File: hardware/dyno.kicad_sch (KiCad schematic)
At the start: 10 parts, among them J1 Battery, J2 Load cell, SW1 B3W-1000, U1 XIAO-ESP32-C3-SMD, U2 HX711

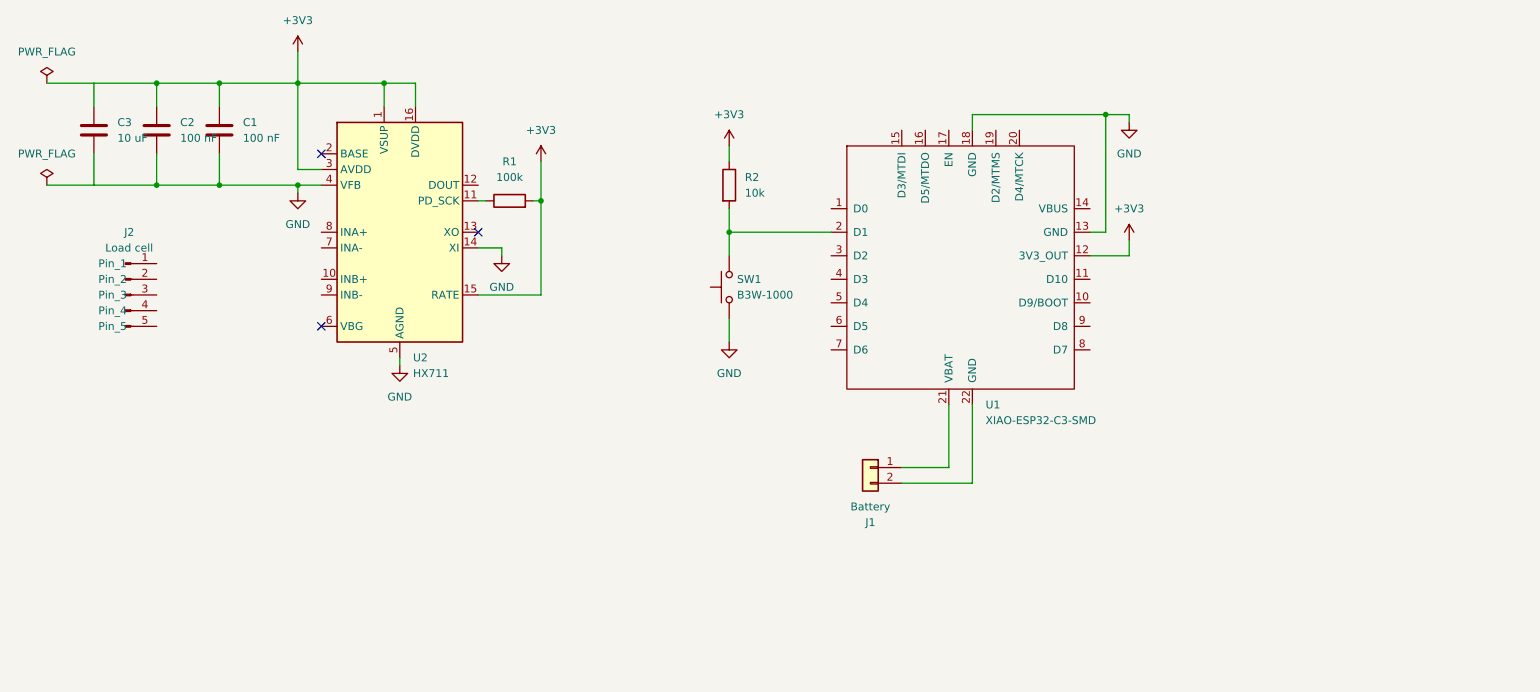
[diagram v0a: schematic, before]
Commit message: wire mcu and amp
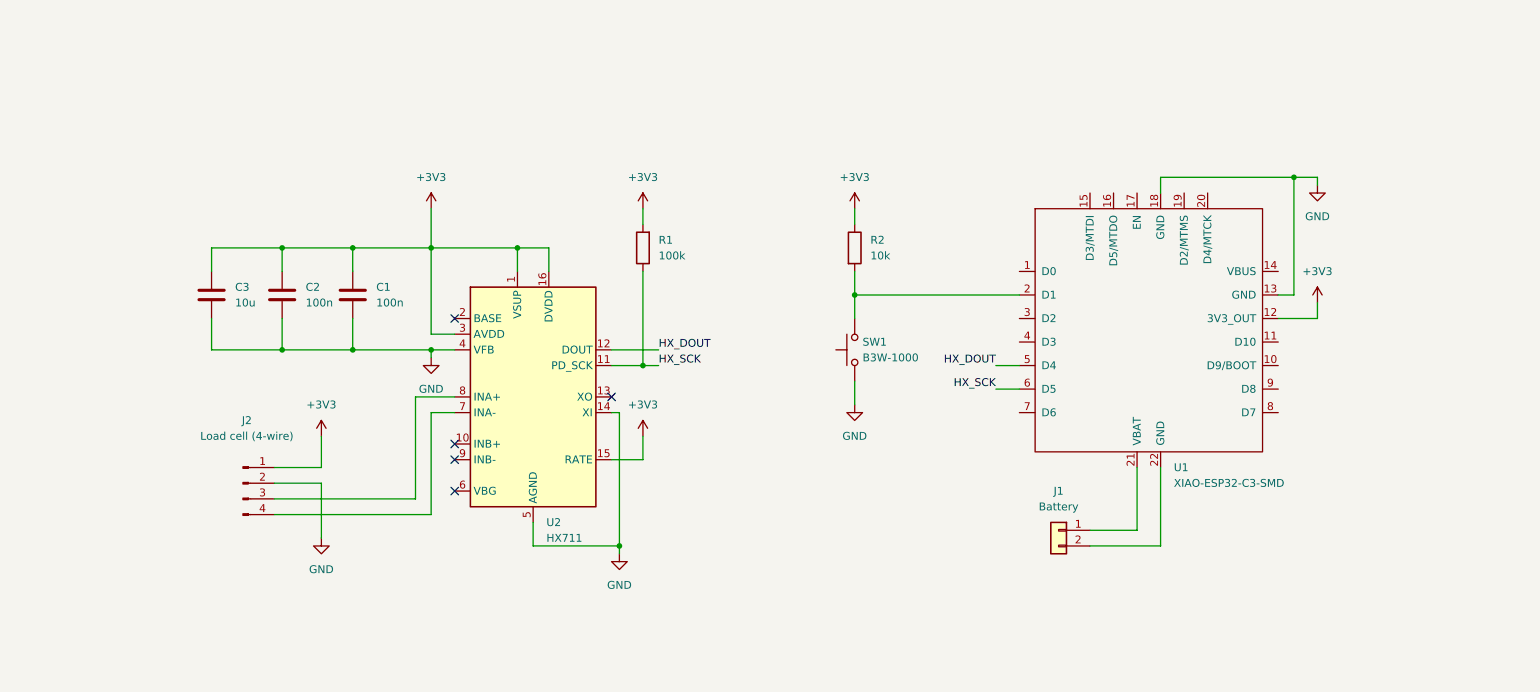
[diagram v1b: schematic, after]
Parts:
- C1, C2: value 100 nF -> 100n
- C3: value 10 uF -> 10u
- J2: value Load cell -> Load cell (4-wire); footprint (none) -> Connector_JST:JST_SH_SM04B-SRSS-TB_1x04-1MP_P1.00mm_Horizontal; symbol Connector:Conn_01x05_Pin -> Connector:Conn_01x04_Pin
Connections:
- net +3V3: now also J2.1 (Pin_1)
- net GND: now also J2.2 (Pin_2)
- net HX_SCK: now reaches R1.1, U2.11 (PD_SCK)
- net HX_SCK: now also U1.6 (D5)
- net at U2.12 (DOUT): no longer names the net of U2.12 (DOUT)
- net at U2.12 (DOUT): now also U1.5 (D4)
- net at U2.7 (INA-): now also J2.4 (Pin_4)
- net at U2.8 (INA+): now also J2.3 (Pin_3)
- no-connect marks 3 -> 5
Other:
- moved on the sheet: C1, C2, C3, J1, R1, R2, SW1, U1, U2

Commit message: fix ERC errors
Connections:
- net HX_DOUT: now reaches U1.5 (D4), U2.12 (DOUT)
- no-connect marks 5 -> 19

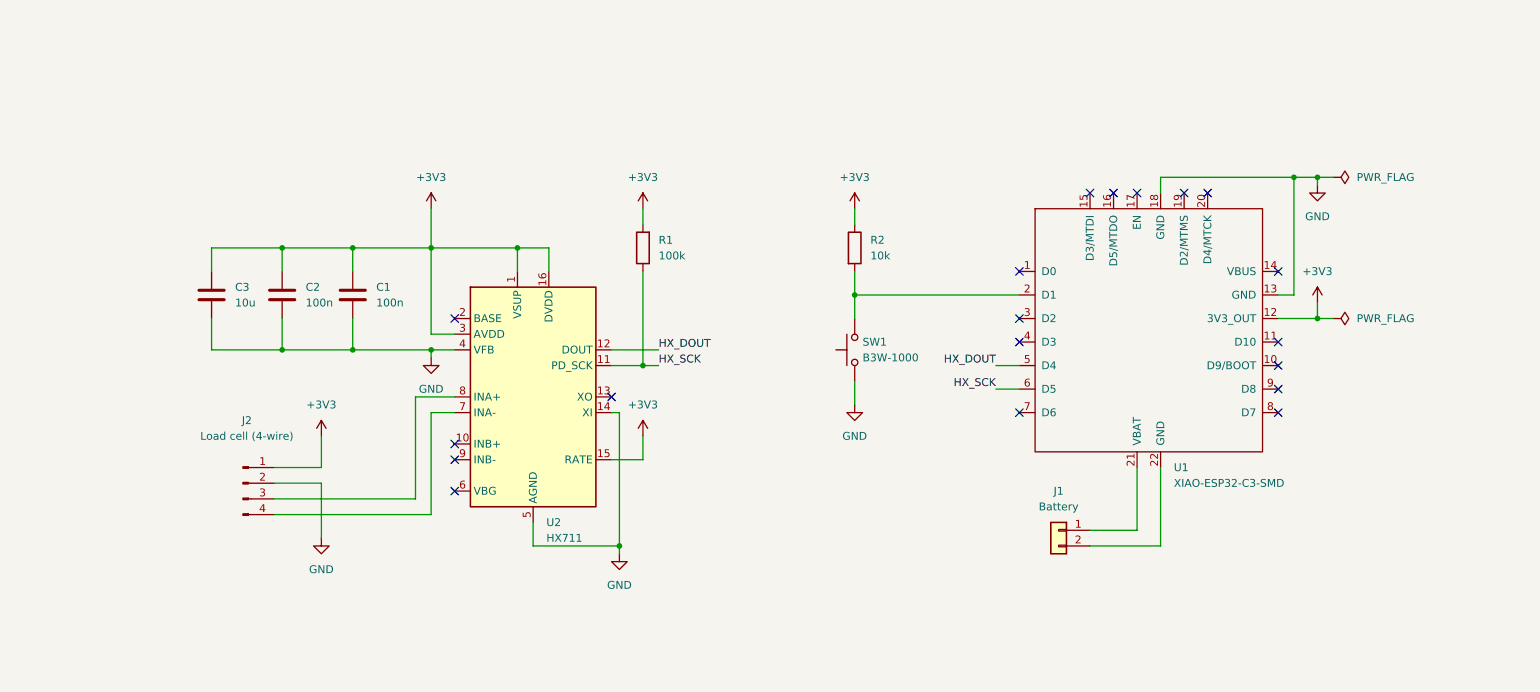
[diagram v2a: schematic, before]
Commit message: clean up schematic
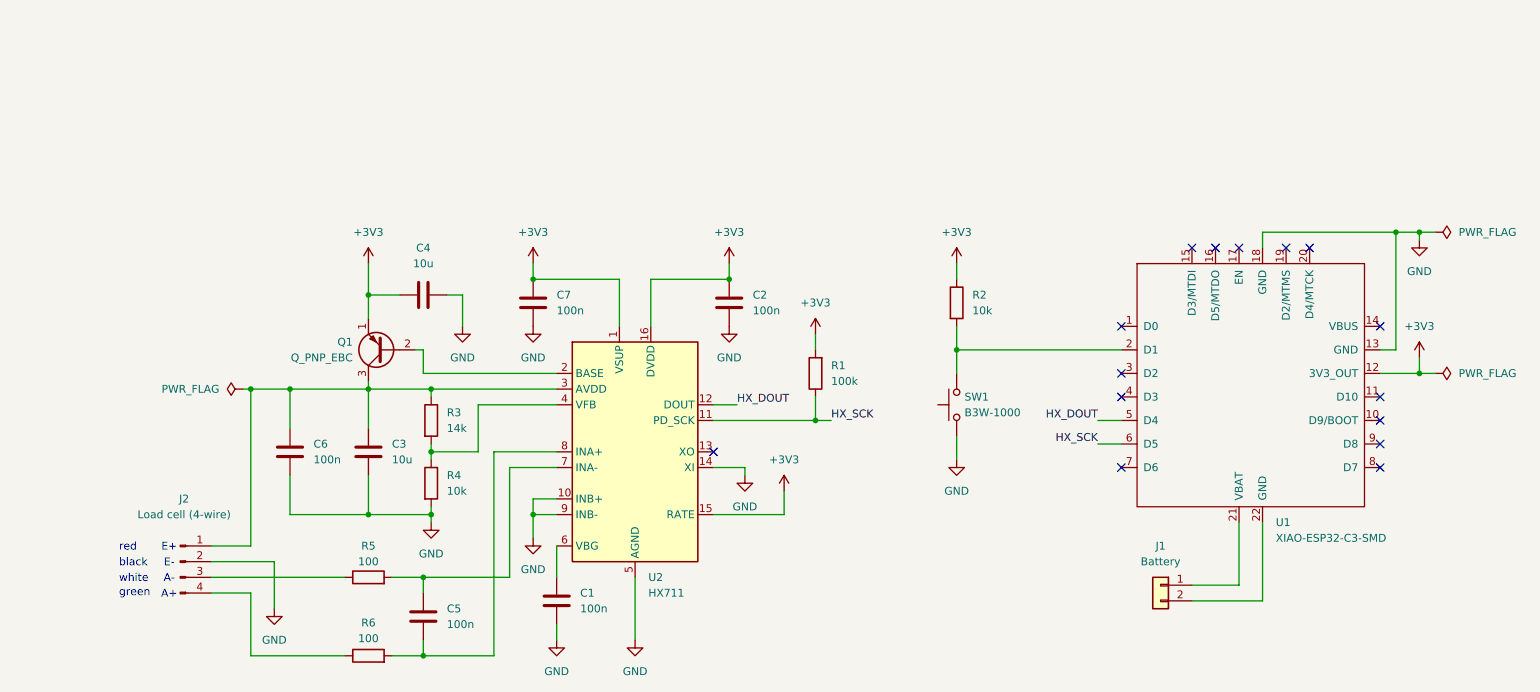
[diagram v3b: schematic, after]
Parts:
- added C4: 10u, symbol Device:C
- added C5, C6, C7: 100n, symbol Device:C
- added Q1: Q_PNP_EBC, symbol Transistor_BJT:Q_PNP_EBC
- added R3: 14k, symbol Device:R
- added R4: 10k, symbol Device:R
- added R5, R6: 100, symbol Device:R
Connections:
- net +3V3: now also C2.2, C4.1, C7.2, Q1.1 (E); no longer C1.1, C2.1, C3.1, J2.1 (Pin_1), U2.3 (AVDD)
- net GND: now also C2.1, U2.10 (INB+), U2.9 (INB-), C4.2, C6.2, C7.1, R4.2; no longer C2.2, U2.4 (VFB)
- net at U2.2 (BASE): now also Q1.2 (B)
- net at U2.6 (VBG): now also C1.1
- net at U2.7 (INA-): now also C5.1, R5.2; no longer J2.4 (Pin_4)
- net at U2.8 (INA+): now also C5.2, R6.2; no longer J2.3 (Pin_3)
- new net: C3.1, C6.1, J2.1 (Pin_1), Q1.3 (C), R3.1, U2.3 (AVDD)
- new net: R3.2, R4.1, U2.4 (VFB)
- new net: J2.3 (Pin_3), R5.1
- new net: J2.4 (Pin_4), R6.1
- no-connect marks 19 -> 15
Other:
- note added: "A+"
- note added: "A-"
- note added: "E+"
- note added: "E-"
- note added: "black"
- note added: "green"
- note added: "red"
- note added: "white"
- moved on the sheet: C1, C2, C3, J1, J2, R1, R2, SW1, U1, U2

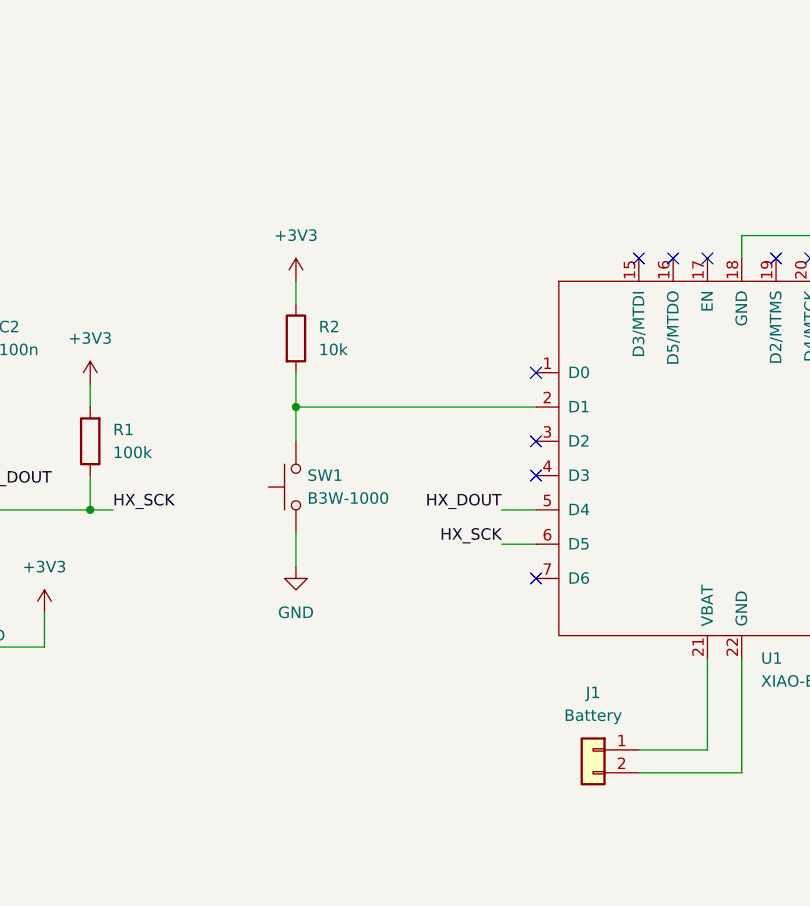
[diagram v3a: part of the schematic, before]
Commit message: add status LED
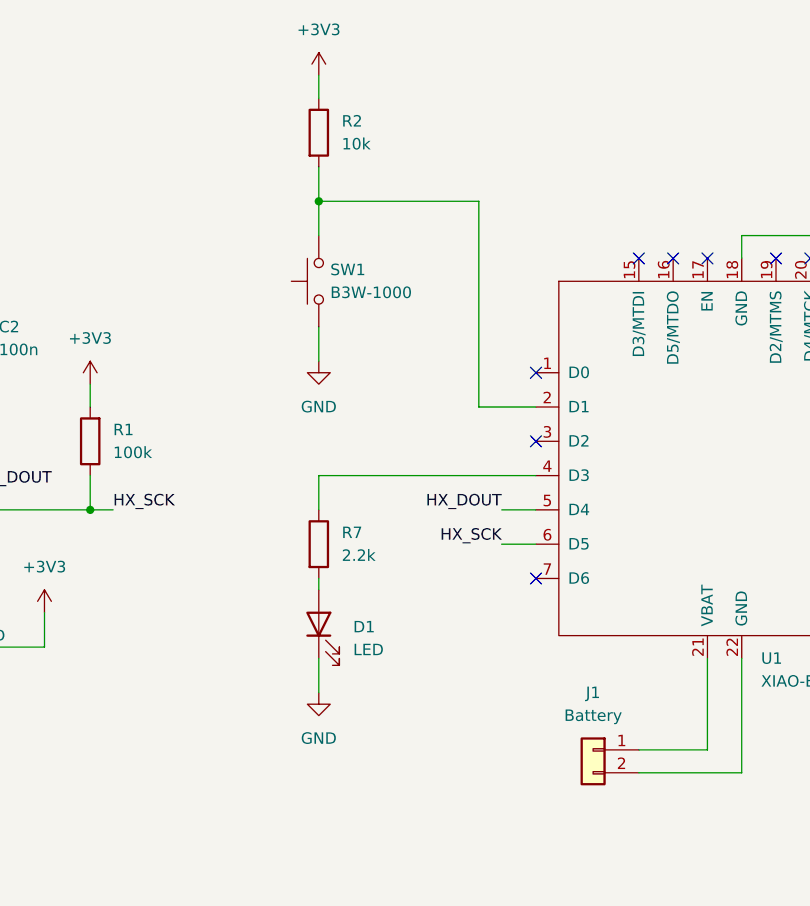
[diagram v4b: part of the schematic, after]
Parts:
- added D1: LED, symbol Device:LED
- added R7: 2.2k, symbol Device:R
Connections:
- net GND: now also D1.1 (K)
- net at U1.4 (D3): now also R7.1
- new net: D1.2 (A), R7.2
- no-connect marks 15 -> 14
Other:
- moved on the sheet: R2, SW1

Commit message: BOM
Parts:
- removed Q1: Q_PNP_EBC, symbol Transistor_BJT:Q_PNP_EBC
- added Q1: MMBT3906LT1G, Package_TO_SOT_SMD:SOT-23, symbol Transistor_BJT:Q_PNP_BEC
- C1, C2, C5, C6, C7: footprint (none) -> Capacitor_SMD:C_0603_1608Metric; JLCPCB Part # (none) -> C14663; MPN (none) -> CC0603KRX7R9BB104; Manufacturer (none) -> YAGEO
- C3, C4: footprint (none) -> Capacitor_SMD:C_0805_2012Metric; JLCPCB Part # (none) -> C15850; MPN (none) -> CL21A106KAYNNNE; Manufacturer (none) -> Samsung Electro-Mechanics
- D1: footprint (none) -> LED_SMD:LED_0603_1608Metric; JLCPCB Part # (none) -> C2286; MPN (none) -> KT-0603R; Manufacturer (none) -> Hubei KENTO Elec
- J1: footprint Connector_JST:JST_PH_S2B-PH-K_1x02_P2.00mm_Horizontal -> Connector_JST:JST_PH_S2B-PH-SM4-TB_1x02-1MP_P2.00mm_Horizontal; JLCPCB Part # (none) -> C295747; MPN (none) -> S2B-PH-SM4-TB(LF)(SN); Manufacturer (none) -> JST
- J2: JLCPCB Part # (none) -> C160404; MPN (none) -> SM04B-SRSS-TB(LF)(SN); Manufacturer (none) -> JST
- R1: footprint (none) -> Resistor_SMD:R_0603_1608Metric; JLCPCB Part # (none) -> C25803; MPN (none) -> 0603WAF1003T5E; Manufacturer (none) -> UNI-ROYAL(Uniroyal Elec)
- R2, R4: footprint (none) -> Resistor_SMD:R_0603_1608Metric; JLCPCB Part # (none) -> C25804; MPN (none) -> 0603WAF1002T5E; Manufacturer (none) -> UNI-ROYAL(Uniroyal Elec)
- R3: footprint (none) -> Resistor_SMD:R_0603_1608Metric; JLCPCB Part # (none) -> C22803; MPN (none) -> 0603WAF1402T5E; Manufacturer (none) -> UNI-ROYAL(Uniroyal Elec)
- R5, R6: footprint (none) -> Resistor_SMD:R_0603_1608Metric; JLCPCB Part # (none) -> C22775; MPN (none) -> 0603WAF1000T5E; Manufacturer (none) -> UNI-ROYAL(Uniroyal Elec)
- R7: footprint (none) -> Resistor_SMD:R_0603_1608Metric; JLCPCB Part # (none) -> C4190; MPN (none) -> 0603WAF2201T5E; Manufacturer (none) -> UNI-ROYAL(Uniroyal Elec)
- SW1: value B3W-1000 -> B3U-1000P; footprint Button_Switch_THT:SW_PUSH_6mm_H4.3mm -> Button_Switch_SMD:SW_SPST_B3U-1000P; JLCPCB Part # (none) -> C231329; MPN (none) -> B3U-1000P; Manufacturer (none) -> Omron Electronics
- U1: JLCPCB Part # (none) -> C9900071238; MPN (none) -> XIAO-ESP32-C3; Manufacturer (none) -> JLCPCB Assembly
- U2: JLCPCB Part # (none) -> C6705483; MPN (none) -> HX711; Manufacturer (none) -> Avia Semicon (Xiamen)
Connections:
- net +3V3: now also Q1.2 (E)
- net at U2.2 (BASE): now also Q1.1 (B)
- net at C3.1, C6.1, J2.1 (Pin_1)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: now also Q1.3 (C)

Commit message: Correct XIAO part number for JLCPCB
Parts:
- U1: JLCPCB Part # C9900071238 -> C18212168; MPN XIAO-ESP32-C3 -> 113991054
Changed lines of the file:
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@@
 			)
 		)
-		(property "JLCPCB Part #" "C9900071238"
+		(property "JLCPCB Part #" "C18212168"
 			(at 224.79 93.98 0)
 			(hide yes)
@@
 			)
 		)
-		(property "MPN" "XIAO-ESP32-C3"
+		(property "MPN" "113991054"
 			(at 224.79 93.98 0)
 			(hide yes)
